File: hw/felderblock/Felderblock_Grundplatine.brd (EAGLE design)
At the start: 100 x 78 mm, 54 parts, among them IC2 LM2936, IC3 ULN2803, IC4 MCP2300X/P, J1 RJ11, J2 RJ11, M1 ARDUINO-NANO-3.0, T2 BC337, X1 TASTENSPERRE1, X2 TASTENSPERRE2, X3 SCHL-SPERRE, X5 ANSCHALTER

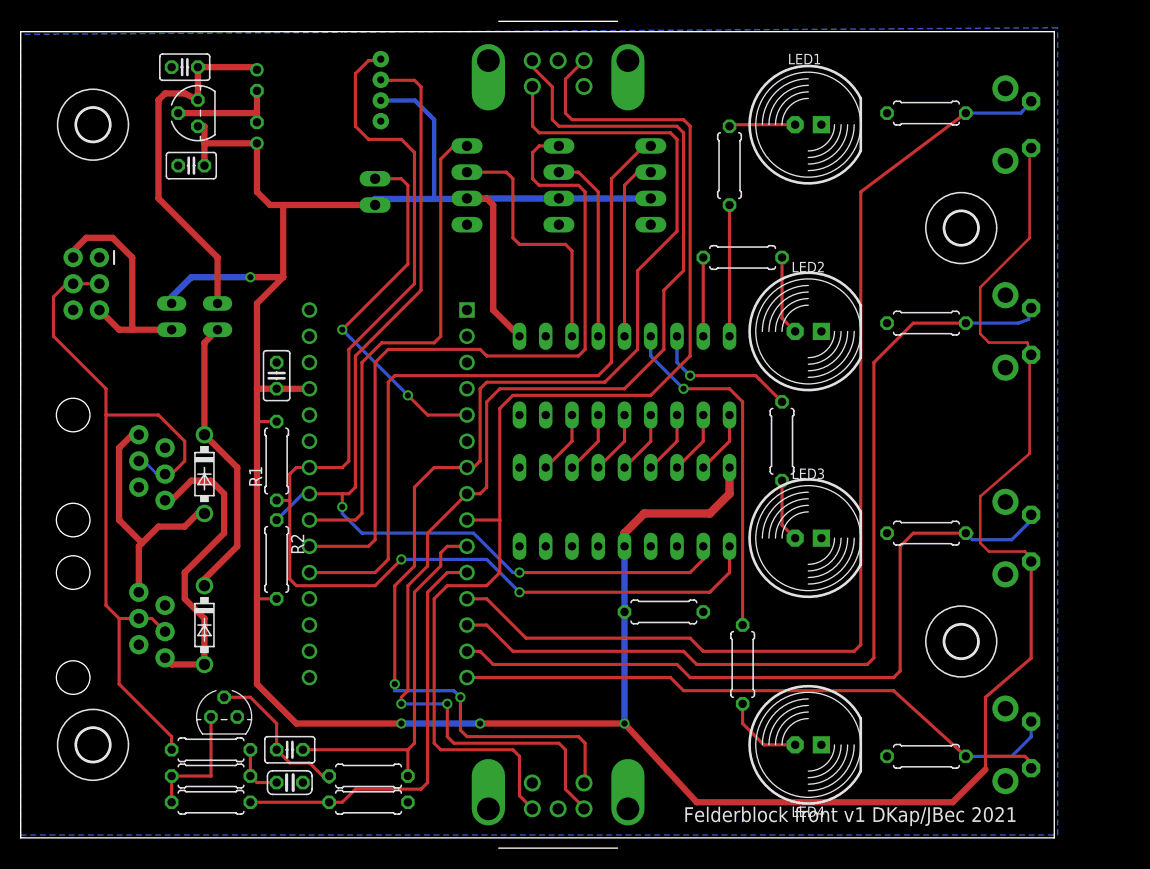
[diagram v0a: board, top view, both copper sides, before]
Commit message: corrected errors
LEDs connections corrected, address for MCP23008 corrected, reset for MCP23008 corrected
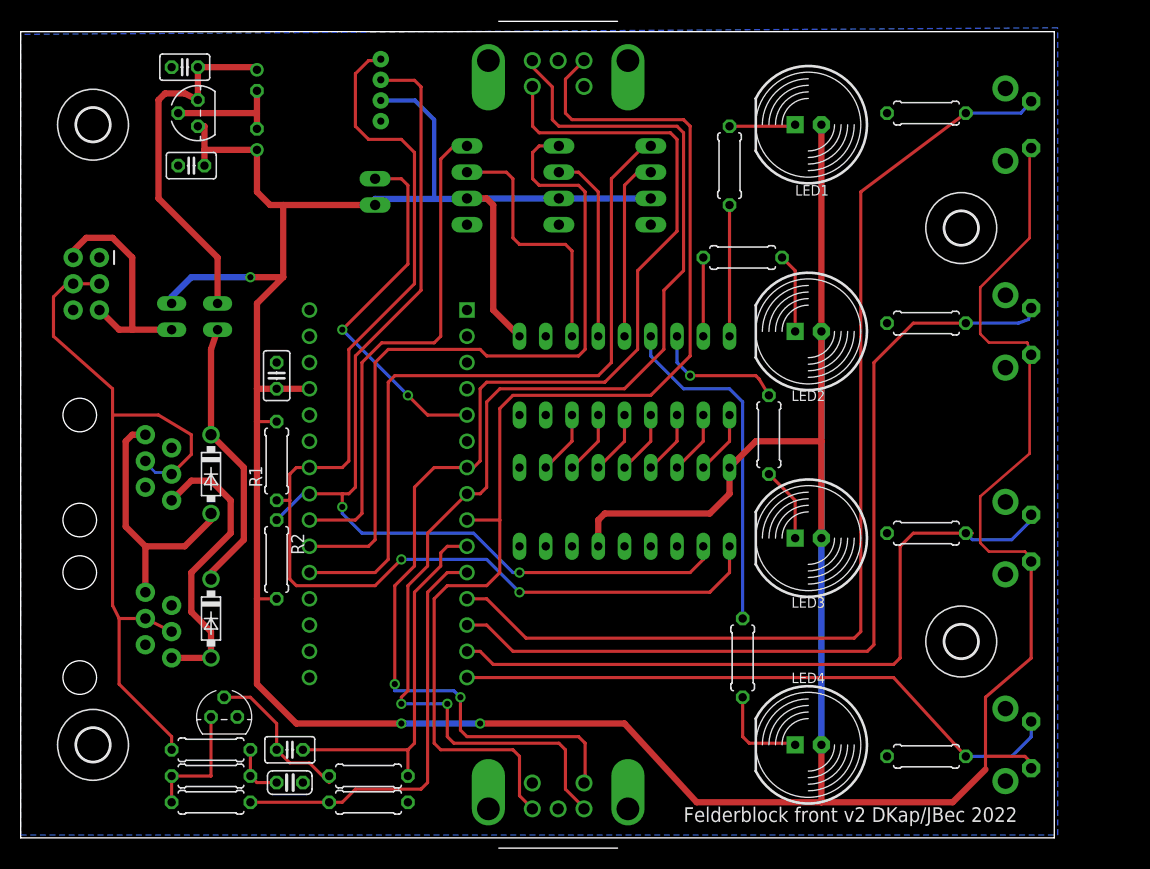
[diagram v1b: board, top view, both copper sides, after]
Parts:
- removed R15: 1k, resistor:0207/7
- moved R13 1.42 mm to (72.4, 40.0)
- moved D1 0.90 mm to (18.4, 22.2)
- moved C5 0.64 mm to (22.9, 68.6)
- moved J1 0.63 mm to (5.71, 21.6)
- moved J2 0.63 mm to (5.71, 36.8)
- moved D2 0.63 mm to (18.4, 36.2)
- moved R14 0.63 mm to (69.8, 18.4)
- turned LED1 to 180 degrees
- turned LED2 to 180 degrees
- turned LED3 to 180 degrees
- turned LED4 to 180 degrees
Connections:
- removed net N$5: LED2.A, R12.2
- removed net N$8: LED3.A, R13.2
- removed net N$9: LED4.A, R14.2
- new net N$1: LED1.K, R11.2
- new net N$2: LED2.K, R12.2
- new net N$3: LED3.K, R13.2
- net +5V: now also IC4.6, LED1.A, LED2.A, LED3.A, LED4.A; no longer IC4.5, R15.2
- net GND: now also IC4.5; no longer IC4.6, LED1.K, LED2.K, LED3.K, LED4.K, R15.1
- net N$4: now also LED4.K, R14.2; no longer LED1.A, R11.2
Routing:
- net +5V: track 341.5 -> 422.5 mm, vias 4 -> 3
- net N$9: track 7.84 -> 0.00 mm
- net N$2: track 0.00 -> 7.68 mm
- net N$5: track 7.68 -> 0.00 mm
- net N$3: track 0.00 -> 7.25 mm
- net N$1: track 0.00 -> 6.50 mm
- net N$8: track 6.09 -> 0.00 mm
- net N$4: track 6.41 -> 9.22 mm
- net FELD2_SW: track 87.5 -> 85.7 mm
- net FELD3_SW: track 70.6 -> 68.8 mm
- net FELD1_SW: track 103.8 -> 102.0 mm
- net FELD3_LEDD: track 14.3 -> 13.0 mm
- net RS1: track 30.0 -> 28.7 mm
- net LOCONET: track 74.8 -> 76.0 mm
- net N$6: track 27.9 -> 26.9 mm
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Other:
- board text added: "Felderblock front v2 DKap/JBec 2022"
- board text removed: "Felderblock front v1 DKap/JBec 2021"

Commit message: moved components to backside
- Components of main panel moved to backside
-  corrected connections for MCP on Hebelplatine
- added address jumpers on Hebelplatine
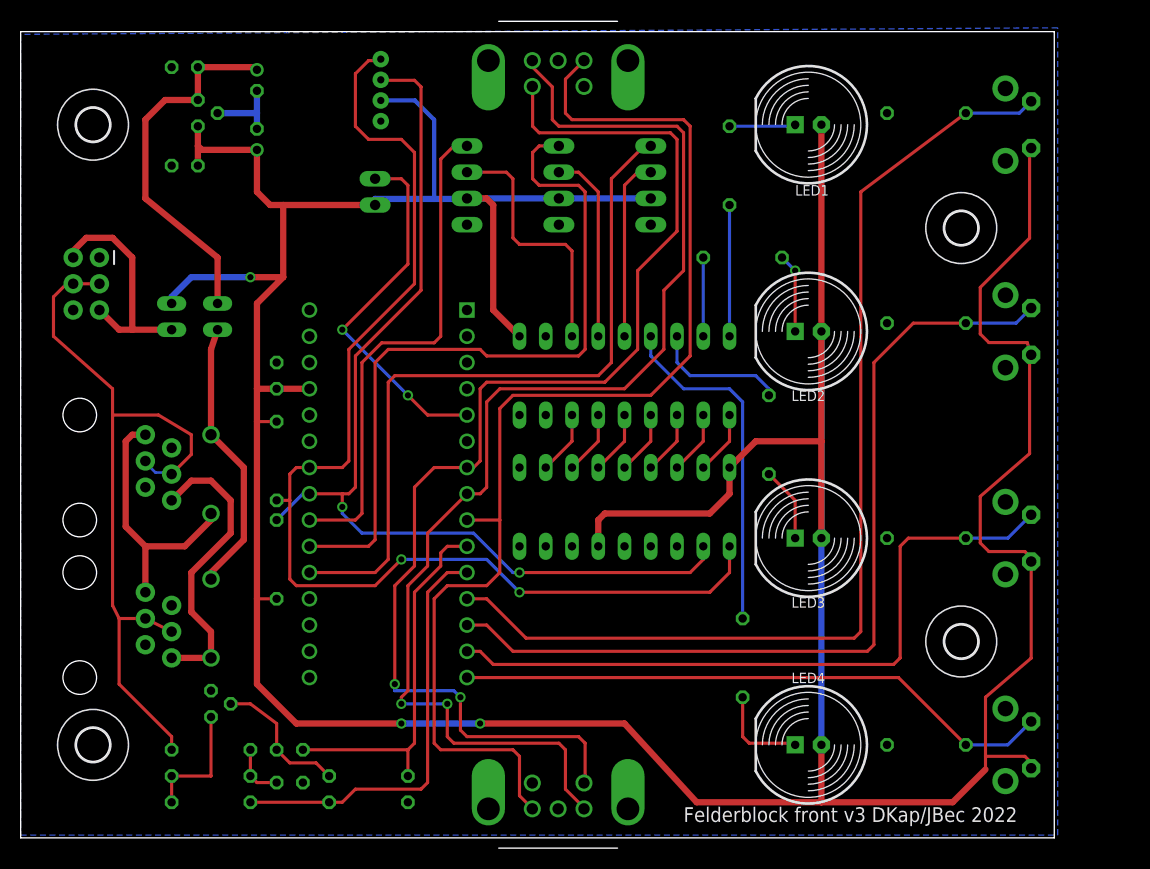
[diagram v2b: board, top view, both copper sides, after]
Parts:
- moved T2 1.80 mm to (18.4, 14.0), flipped to the bottom, turned to 90 degrees
- moved R7 1.11 mm to (87.6, 10.0), flipped to the bottom, turned to 0 degrees
- moved C2 0.64 mm to (15.9, 66.0), flipped to the bottom, turned to 0 degrees
- moved R8 0.48 mm to (87.6, 30.0), flipped to the bottom, turned to 0 degrees
- flipped C1 to the bottom, turned to 0 degrees
- flipped C3 to the bottom
- flipped C6 to the bottom, turned to 180 degrees
- flipped C7 to the bottom, turned to 0 degrees
- flipped D1 to the bottom
- flipped D2 to the bottom
- flipped IC2 to the bottom
- flipped R1 to the bottom
- flipped R10 to the bottom, turned to 0 degrees
- flipped R11 to the bottom
- flipped R12 to the bottom, turned to 180 degrees
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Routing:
- net GND: track 11.3 -> 7.49 mm
- net FELD4_SW: track 60.2 -> 58.2 mm
- net BASE: track 15.7 -> 13.8 mm
- net FELD3_SW: track 68.8 -> 67.4 mm
- net N$7: track 35.4 -> 36.1 mm
- net FELD3_LEDD: track 13.0 -> 13.1 mm, vias 1 -> 0
- net N$2: vias 0 -> 1
- net N$1: vias 0 -> 1
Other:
- board text added: "Felderblock front v3 DKap/JBec 2022"
- board text removed: "Felderblock front v2 DKap/JBec 2022"

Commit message: Changed to PCA9685
- Changed LED-driver to PCA9685
- Now two LED per field
- Use LN-circuit with comparator
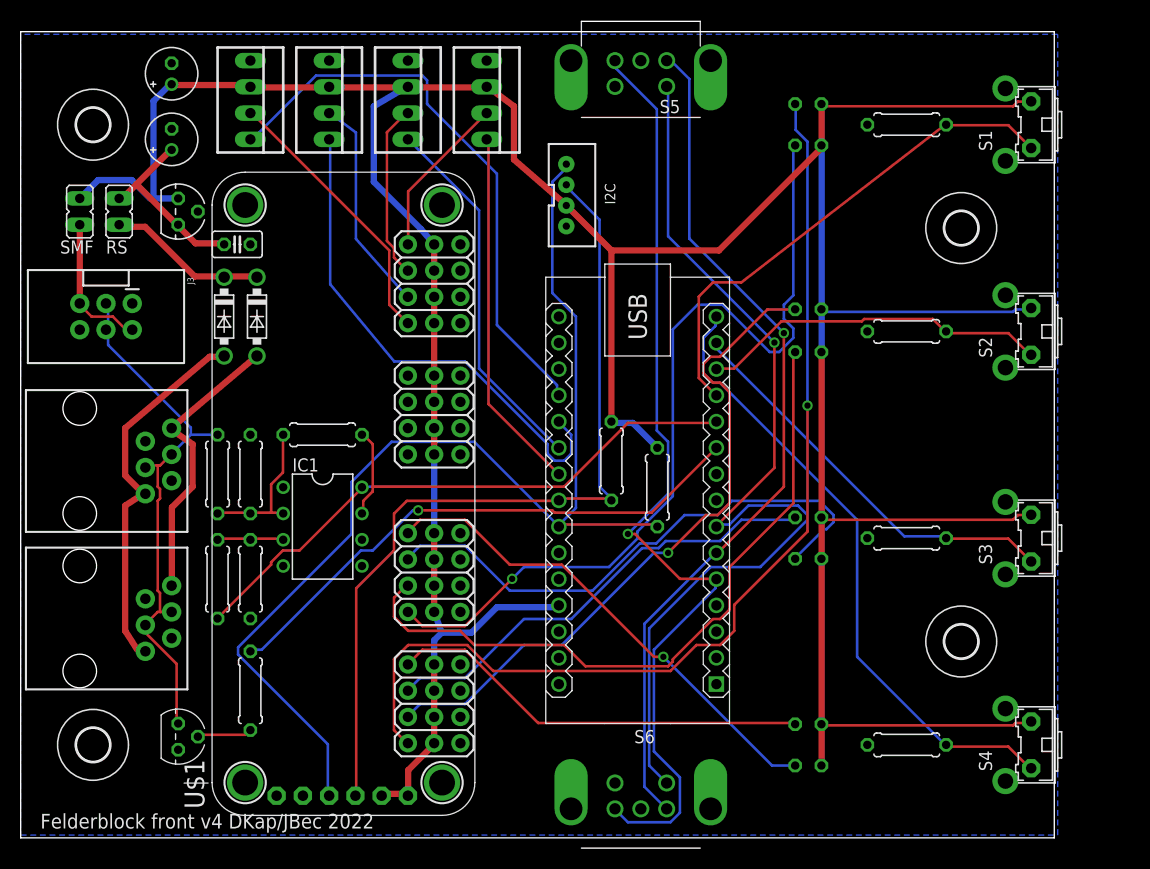
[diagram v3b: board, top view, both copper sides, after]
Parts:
- removed C2, C3: 100nF, resistor:C025-025X050
- removed C6: 47pF, resistor:C025-024X044
- removed C7: 1nF, resistor:C025-025X050
- removed IC3: ULN2803, uln-udn:DIL18
- removed IC4: MCP2300X/P, adafruit:DIL18
- removed R11, R12, R13, R14: 1k, resistor:0207/7
- added IC1: LM311N, linear:DIL08
- added LED5, LED6, LED7, LED8: (no value), led:LED3MM
- added R3: 4.7k, resistor:0207/7
- added U$1: ADA9685-STACK, ada9685:ADA9685-STACK
- LED1, LED2, LED3, LED4: device led:LED10MM -> led:LED3MM
- R16: value 12R -> 47k
- R17: value 12R -> 150k
- R18: value 130K -> 10k
- R19: value 47k -> 22k
- R20: value 3K3 -> 220k
- X3: device con-molex:22-23-2021 -> con-molex:22-23-2041
- moved X1 39.6 mm to (22.2, 72.4), flipped to the top, turned to 270 degrees
- moved R1 36.9 mm to (61.6, 34.9), flipped to the top
- moved R2 33.8 mm to (57.1, 37.5), flipped to the top, turned to 90 degrees
- moved R20 33.3 mm to (29.2, 40.0), flipped to the top, turned to 180 degrees
- moved D1 29.5 mm to (22.9, 51.4), flipped to the top
- moved R17 29.5 mm to (22.2, 36.2), flipped to the top, turned to 270 degrees
- moved R16 26.7 mm to (19.1, 36.2), flipped to the top, turned to 90 degrees
- moved R19 24.4 mm to (22.2, 26.0), flipped to the top, turned to 90 degrees
- moved M1 24.1 mm to (59.7, 33.7), flipped to the top, turned to 270 degrees
- moved X2 23.7 mm to (29.8, 72.4), flipped to the top, turned to 270 degrees
- moved R18 21.6 mm to (19.1, 26.0), flipped to the top, turned to 270 degrees
- moved I2C 21.6 mm to (53.3, 63.2), flipped to the top
- moved C1 17.9 mm to (21.0, 58.4), flipped to the top
- moved D2 15.3 mm to (19.7, 51.4), flipped to the top
- moved RS 13.9 mm to (9.53, 61.6), flipped to the top
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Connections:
- removed net AS_LEDD: IC3.12, X5.3
- removed net FELD1_LED: IC3.1, IC4.17
- removed net FELD1_LEDD: IC3.18, R11.1
- removed net FELD2_LED: IC3.2, IC4.16
- removed net FELD2_LEDD: IC3.17, R12.1
- removed net FELD3_LED: IC3.3, IC4.15
- removed net FELD3_LEDD: IC3.16, R13.1
- removed net FELD4_LED: IC3.4, IC4.14
- removed net FELD4_LEDD: IC3.15, R14.1
- removed net LN_INTERN: R17.2, R18.2, T2.3
- removed net N$1: LED1.K, R11.2
- removed net N$11: C6.1, R16.2, R17.1
- removed net N$2: LED2.K, R12.2
- removed net N$3: LED3.K, R13.2
- removed net N$4: LED4.K, R14.2
- removed net SCHL_SPERRE: M1.J1.5, X3.2
- removed net TSP1_LEDD: IC3.14, X1.3
- removed net TSP2_LEDD: IC3.13, X2.3
- new net FELD1_LED_RD: LED1.K, U$1.3
- new net FELD1_LED_WS: LED5.K, U$1.33
- new net FELD2_LED_RD: LED2.K, U$1.6
- new net FELD2_LED_WS: LED6.K, U$1.36
- new net FELD3_LED_RD: LED3.K, U$1.9
- new net FELD3_LED_WS: LED7.K, U$1.39
- new net FELD4_LED_RD: LED4.K, U$1.12
- new net FELD4_LED_WS: LED8.K, U$1.42
- new net N$5: IC1.2, R16.1, R17.2, R20.2
- new net N$8: IC1.3, R18.1, R19.2
- new net SCHL_SP_LED: U$1.51, X3.3
- new net SCHL_SP_SW: M1.J2.10, X3.4
- net +5V: now also IC1.8, LED5.A, LED6.A, LED7.A, LED8.A, R18.2, U$1.11, U$1.19, U$1.2, U$1.20, U$1.32, U$1.35, U$1.38, U$1.41, U$1.44, U$1.47, U$1.5, U$1.50, U$1.53, U$1.56, U$1.59, U$1.62, U$1.65, U$1.8, X3.2; no longer C2.1, C3.1, IC3.10, IC4.18, IC4.6, X3.1
- net AS_LED: now also U$1.54, X5.3; no longer IC3.7, IC4.11
- net BASE: now also R3.2; no longer C7.2, R20.2
- net GND: now also IC1.1, IC1.4, R17.1, U$1.1, U$1.10, U$1.24, U$1.31, U$1.34, U$1.37, U$1.4, U$1.40, U$1.43, U$1.46, U$1.49, U$1.52, U$1.55, U$1.58, U$1.61, U$1.64, U$1.7, X3.1; no longer C2.2, C3.2, C6.2, IC3.9, IC4.3, IC4.4, IC4.5, IC4.9
- net LN_RX: now also IC1.7, R20.1; no longer R18.1, R19.2
- net LN_TX: now also R3.1; no longer C7.1, R20.1
- net LOCONET: now also R16.2, T2.3; no longer R16.1
- net MI_FWD: now also M1.J1.5; no longer M1.J1.9
- net MI_REV: now also M1.J1.6; no longer M1.J1.8
- net SCL: now also U$1.22; no longer IC4.1
- net SDA: now also U$1.21; no longer IC4.2
- net TSP1_LED: now also U$1.45, X1.3; no longer IC3.5, IC4.13
- net TSP1_SW: now also M1.J2.12; no longer M1.J2.11
- net TSP2_LED: now also U$1.48, X2.3; no longer IC3.6, IC4.12
- net TSP2_SW: now also M1.J2.11; no longer M1.J2.10
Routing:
- net FELD1_LED_RD: track 0.00 -> 99.2 mm, vias 0 -> 1
- net FELD1_LED_WS: track 0.00 -> 82.5 mm, vias 0 -> 1
- net FELD2_LED_WS: track 0.00 -> 68.0 mm
- net FELD2_LED_RD: track 0.00 -> 65.7 mm, vias 0 -> 1
- net FELD3_LED_WS: track 0.00 -> 53.7 mm
- net FELD1_SW: track 102.0 -> 49.1 mm
- net FELD2_SW: track 85.4 -> 33.9 mm
- net FELD4_LED_WS: track 0.00 -> 47.9 mm, vias 0 -> 1
- net FELD3_LED_RD: track 0.00 -> 44.4 mm
- net FELD4_LED_RD: track 0.00 -> 41.0 mm
- net +5V: track 422.7 -> 384.3 mm, vias 3 -> 0
- net MI_REV: track 120.1 -> 83.9 mm, vias 2 -> 1
- net SCHL_SP_SW: track 0.00 -> 35.9 mm
- net SCHL_SPERRE: track 35.5 -> 0.00 mm, vias 2 -> 0
- net FELD4_LEDD: track 33.6 -> 0.00 mm
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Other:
- board text added: "Felderblock front v4 DKap/JBec 2022"
- board text removed: "Felderblock front v3 DKap/JBec 2022"

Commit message: Rearranged order of LED and switches
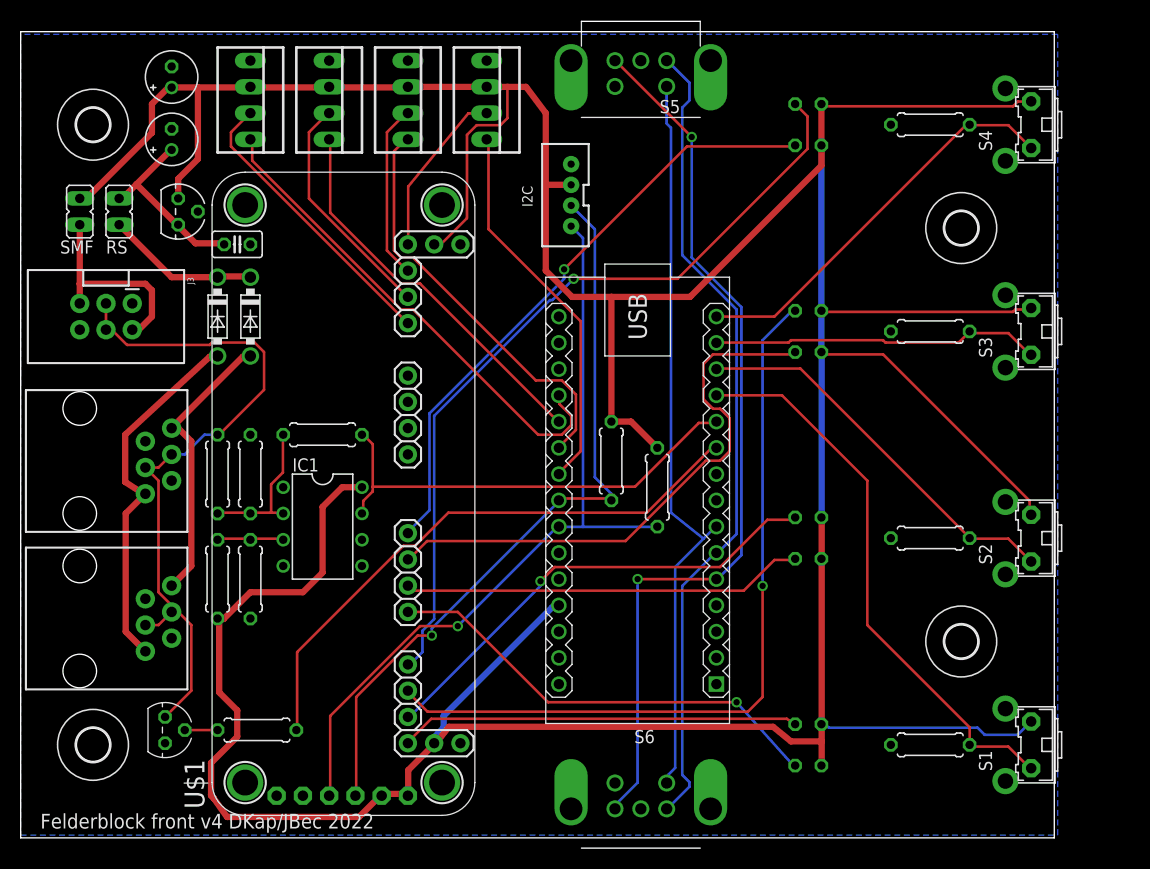
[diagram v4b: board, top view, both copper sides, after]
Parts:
- moved R10 60.0 mm to (88.0, 10.0)
- moved R7 60.0 mm to (88.0, 70.0)
- moved LED1 60.0 mm to (76.2, 12.0)
- moved LED4 60.0 mm to (76.2, 72.0)
- moved LED5 60.0 mm to (76.2, 8.00)
- moved LED8 60.0 mm to (76.2, 68.0)
- moved S1 60.0 mm to (96.5, 10.0)
- moved S4 60.0 mm to (96.5, 70.0)
- moved LED2 20.1 mm to (76.2, 32.0)
- moved R8 20.1 mm to (88.0, 50.0)
- moved R9 20.1 mm to (88.0, 30.0)
- moved LED3 20.0 mm to (76.2, 52.0)
- moved LED6 20.0 mm to (76.2, 28.0)
- moved LED7 20.0 mm to (76.2, 48.0)
- moved S2 20.0 mm to (96.5, 30.0)
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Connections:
- net +5V: no longer U$1.11, U$1.32, U$1.35, U$1.38, U$1.41, U$1.44, U$1.47, U$1.5, U$1.50, U$1.56, U$1.59, U$1.62, U$1.65, U$1.8
- net GND: no longer U$1.10, U$1.31, U$1.34, U$1.37, U$1.4, U$1.40, U$1.43, U$1.46, U$1.49, U$1.55, U$1.58, U$1.61, U$1.64, U$1.7
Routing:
- net FELD1_LED_RD: track 99.2 -> 38.6 mm, vias 1 -> 0
- net +5V: track 384.3 -> 435.5 mm
- net FELD1_LED_WS: track 82.5 -> 43.8 mm
- net FELD4_LED_RD: track 41.0 -> 77.1 mm, vias 0 -> 1
- net SCL: track 110.7 -> 76.8 mm, vias 0 -> 1
- net FELD3_LED_RD: track 44.4 -> 74.6 mm, vias 0 -> 1
- net FELD2_LED_WS: track 68.0 -> 38.9 mm
- net MI_SW: track 95.1 -> 72.3 mm, vias 1 -> 0
- net FELD4_SW: track 61.4 -> 39.2 mm
- net FELD2_LED_RD: track 65.7 -> 45.9 mm
- net LOCONET: track 53.2 -> 67.6 mm
- net TSP2_SW: track 49.3 -> 37.7 mm
- net FELD4_LED_WS: track 47.9 -> 59.1 mm
- net SDA: track 83.0 -> 73.1 mm, vias 0 -> 1
- net TSP1_SW: track 55.6 -> 47.8 mm
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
